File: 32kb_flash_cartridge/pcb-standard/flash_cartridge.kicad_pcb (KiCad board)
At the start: 2 copper layers, 57 x 34.7 mm, 6 parts, among them U1 74HCT00, U2 SST39SF010A

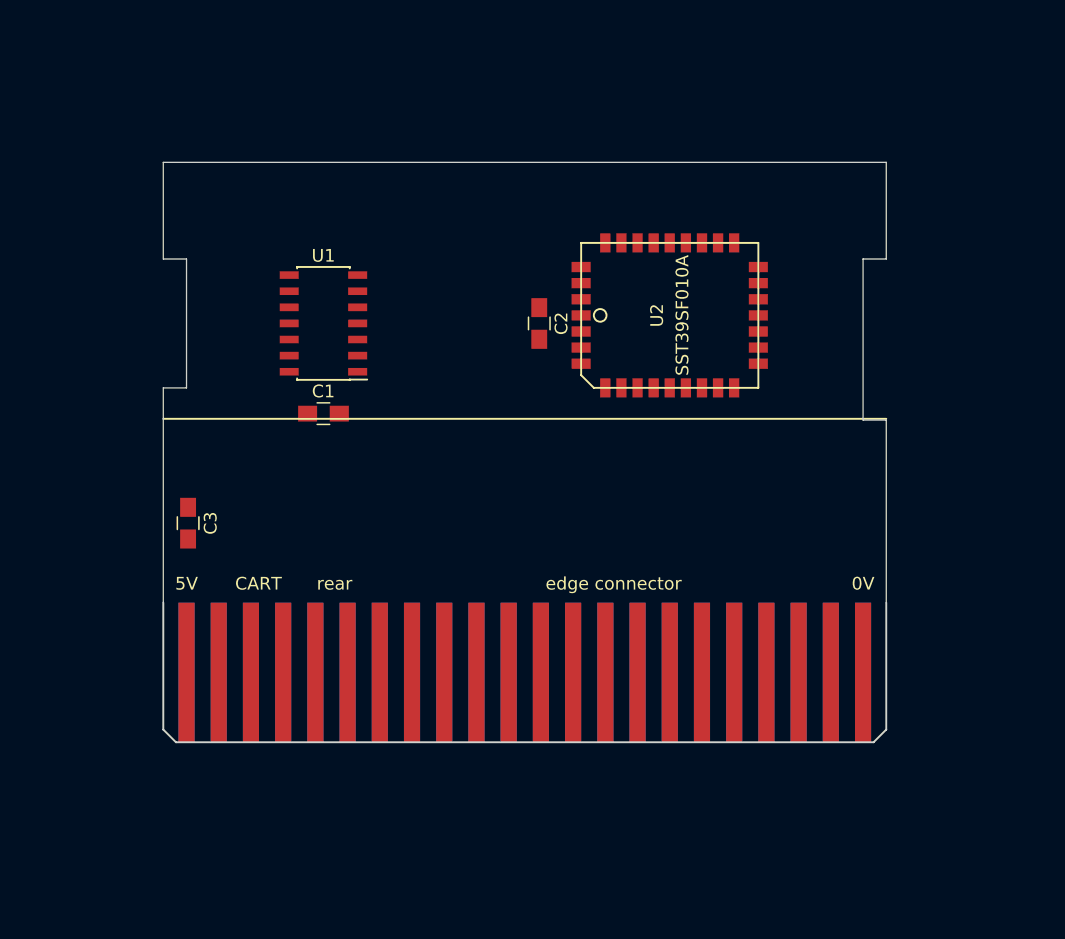
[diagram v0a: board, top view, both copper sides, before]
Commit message: Finished 32kb_flash_cartridge mini and standard board layouts
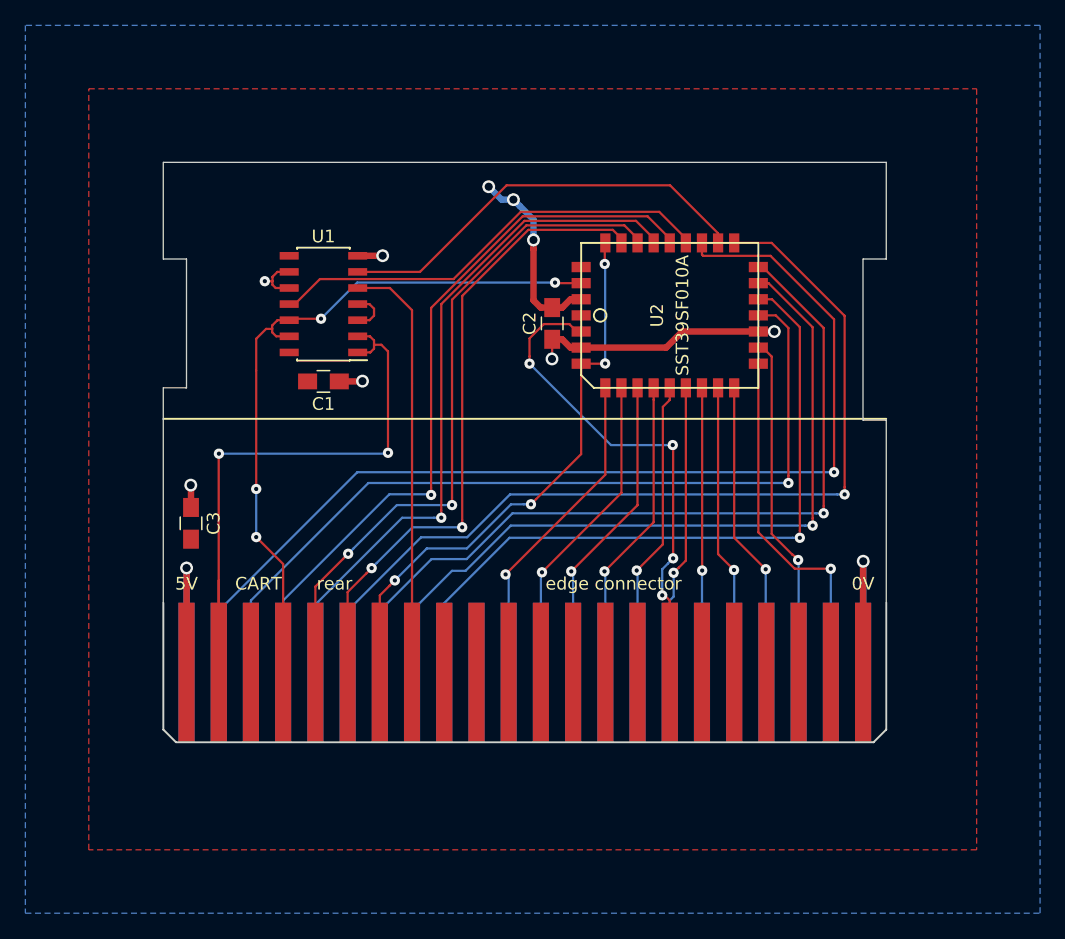
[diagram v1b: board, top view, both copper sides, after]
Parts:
- moved C1 2.54 mm to (63.5, 68.1)
- moved U1 1.52 mm to (63.5, 62.0)
- moved C2 1.02 mm to (81.5, 63.5)
- moved C3 0.23 mm to (53.1, 79.3)
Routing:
- net elk_A10: track 0.00 -> 83.4 mm, vias 0 -> 1
- net elk_D7: track 0.00 -> 73.0 mm, vias 0 -> 1
- net elk_D3: track 0.00 -> 66.9 mm, vias 0 -> 1
- net elk_D6: track 0.00 -> 64.8 mm, vias 0 -> 1
- net elk_D5: track 0.00 -> 60.6 mm, vias 0 -> 1
- net elk_A11: track 0.00 -> 58.5 mm, vias 0 -> 1
- net elk_RnW: track 0.00 -> 56.6 mm, vias 0 -> 4
- net elk_D4: track 0.00 -> 56.4 mm, vias 0 -> 1
- net elk_A9: track 0.00 -> 55.3 mm, vias 0 -> 1
- net elk_A8: track 0.00 -> 54.2 mm, vias 0 -> 2
- net elk_A13: track 0.00 -> 51.1 mm, vias 0 -> 2
- net elk_nOE: track 0.00 -> 50.7 mm, vias 0 -> 2
- net GND: track 0.00 -> 47.1 mm, vias 0 -> 7
- net elk_A12: track 0.00 -> 45.5 mm, vias 0 -> 4
- net elk_ROMQA: track 0.00 -> 39.4 mm, vias 0 -> 4
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- added copper zone on F.Cu, net 5V
- added copper zone on B.Cu, net GND
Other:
- net class Default: clearance 0.2 -> 0.1778; trace_width 0.25 -> 0.1778; via_dia 0.6 -> 0.8128; via_drill 0.4 -> 0.3302
- rule trace_clearance: 0.2 -> 0.1778
- rule trace_min: 0.2 -> 0.1778
- rule via_min_drill: 0.3 -> 0.3302
- rule via_min_size: 0.4 -> 0.8128
- board text added: "Standard-sized Acorn Electron 32kB flash cartridge Phillip Pearson <pp@myelin.co.nz> Copyright (C) 2017 Google Inc https://github.com/google/myelin-acorn-electron-hardware"
